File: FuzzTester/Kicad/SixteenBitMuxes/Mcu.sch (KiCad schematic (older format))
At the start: 20 parts, among them J10 Key Pad JST XH, J11 LCD JST XH, J12 Bypass Switch JST XH, J7 Boot Reset PinHeader, J8 SPI Test PinHeader, J9 SWD_PinHeader, U3 STM32F103C8Tx, Y1 8MHz

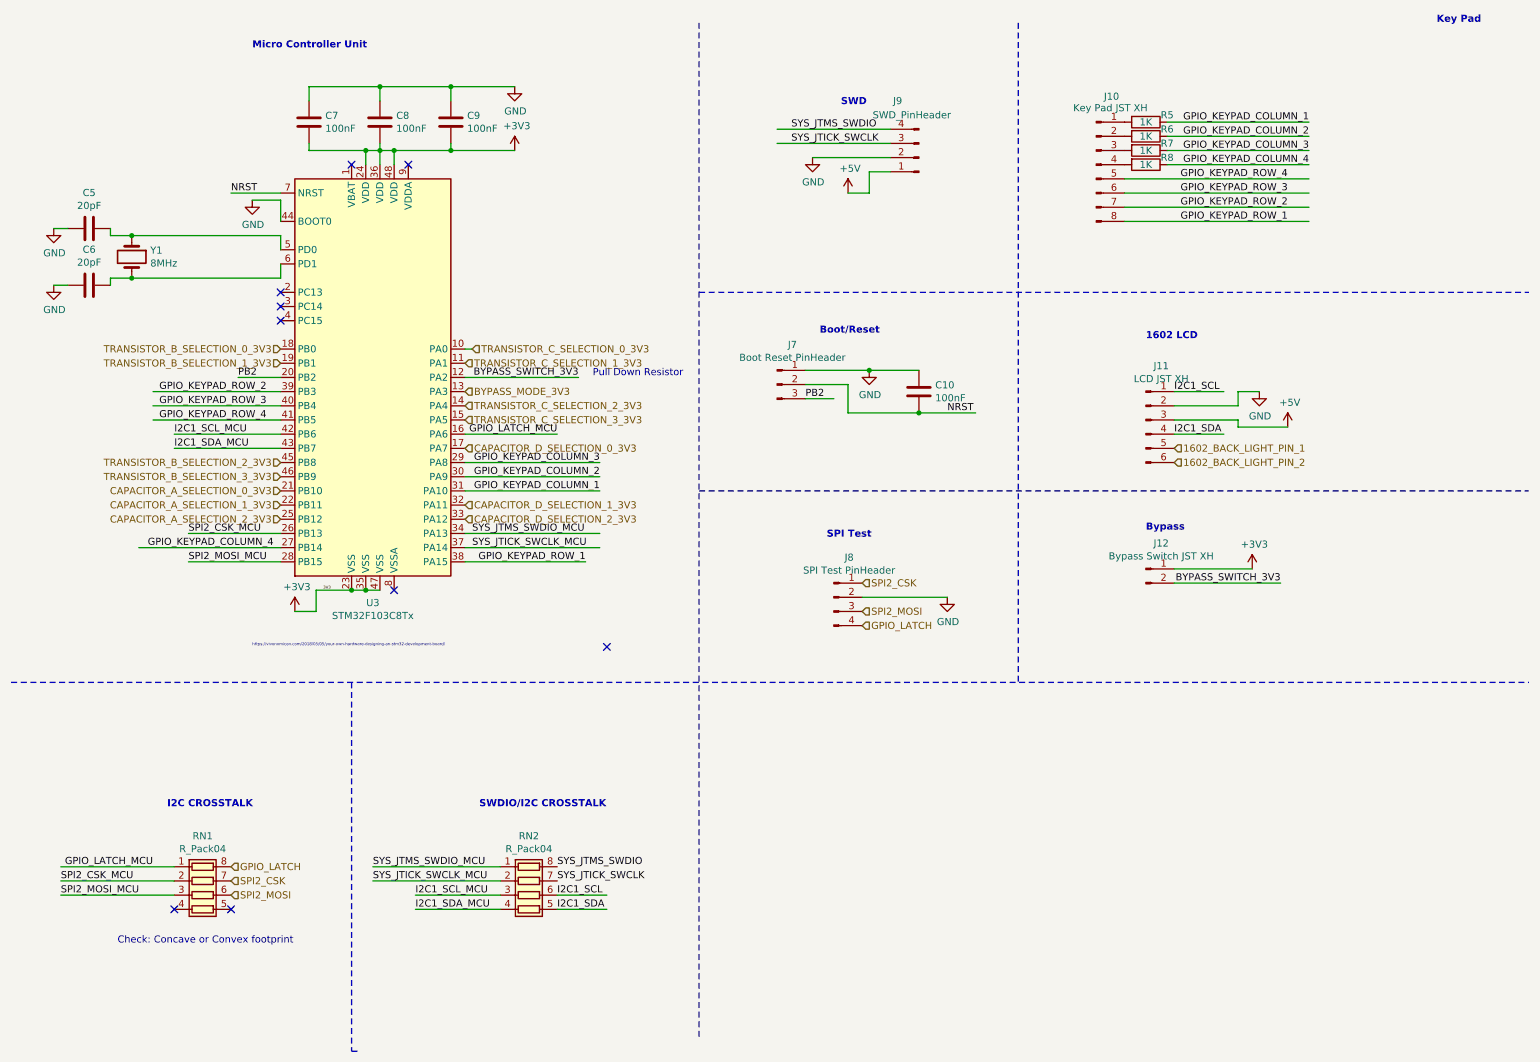
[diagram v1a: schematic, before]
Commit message: Finished (but not beautiful) PCB without SPI and most 8 channel multiplexers.
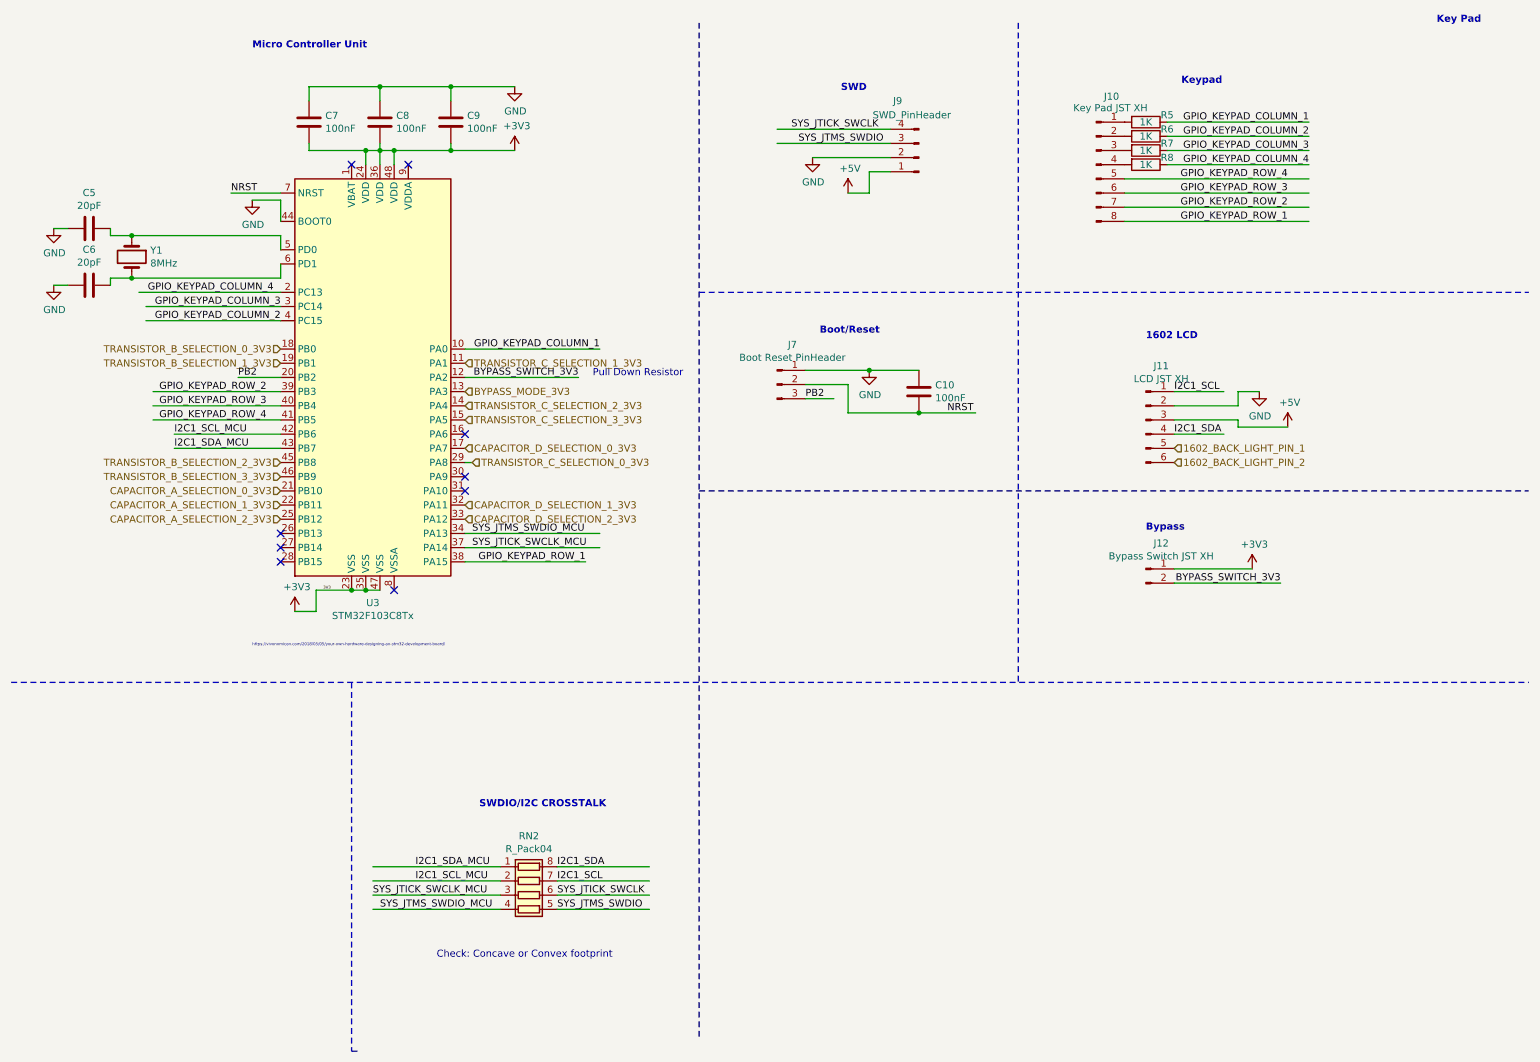
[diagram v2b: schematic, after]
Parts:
- removed J8: SPI Test PinHeader, Connector_PinHeader_2.54mm:PinHeader_1x04_P2.54mm_Vertical, symbol Connector:Conn_01x04_Male
- removed RN1: R_Pack04, Resistor_SMD:R_Array_Convex_4x0603, symbol Device:R_Pack04
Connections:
- net labels removed: GPIO_LATCH, GPIO_LATCH_MCU, SPI2_CSK, SPI2_CSK_MCU, SPI2_MOSI, SPI2_MOSI_MCU
- wire segments 94 -> 89
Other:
- note added: "Keypad\n\n\n"
- note removed: "I2C CROSSTALK\n\n\n"
- note removed: "SPI Test\n\n\n"
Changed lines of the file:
@@
 $Descr A4 11693 8268
 encoding utf-8
-Sheet 6 9
+Sheet 9 9
 Title "Guitar Pedal Effect Fuzz Digitally Controlled"
 Date "2020-04-07"
@@
 	-1   0    0    1
 $EndComp
+Text Label 6050 1400 0    50   ~ 0
+SYS_JTMS_SWDIO
 Text Label 6000 1300 0    50   ~ 0
-SYS_JTMS_SWDIO
-Text Label 6000 1400 0    50   ~ 0
 SYS_JTICK_SWCLK
 $Comp
@@
 Text Notes 6200 2750 0    50   ~ 10
 Boot/Reset\n
-$Comp
-L Connector:Conn_01x04_Male J?
-U 1 1 5EBB7B0E
-P 6300 4600
-AR Path="/5EBB7B0E" Ref="J?"  Part="1"
-AR Path="/5E8F7778/5EBB7B0E" Ref="J?"  Part="1"
-AR Path="/5E8BDF21/5EBB7B0E" Ref="J8"  Part="1"
-F 0 "J8" H 6408 4881 50  0000 C CNN
-F 1 "SPI Test PinHeader" H 6408 4790 50  0000 C CNN
-F 2 "Connector_PinHeader_2.54mm:PinHeader_1x04_P2.54mm_Vertical" H 6300 4600 50  0001 C CNN
-F 3 "~" H 6300 4600 50  0001 C CNN
-	1    6300 4600
-	1    0    0    -1
-$EndComp
-$Comp
-L power:GND #PWR?
-U 1 1 5EBB7B14
-P 7100 4600
-AR Path="/5EBB7B14" Ref="#PWR?"  Part="1"
-AR Path="/5E8F7778/5EBB7B14" Ref="#PWR?"  Part="1"
-AR Path="/5E8BDF21/5EBB7B14" Ref="#PWR023"  Part="1"
-F 0 "#PWR023" H 7100 4350 50  0001 C CNN
-F 1 "GND" H 7105 4427 50  0000 C CNN
-F 2 "" H 7100 4600 50  0001 C CNN
-F 3 "" H 7100 4600 50  0001 C CNN
-	1    7100 4600
-	1    0    0    -1
-$EndComp
-Text Notes 6250 4350 0    50   ~ 10
-SPI Test\n\n\n
-Text HLabel 6500 4500 2    50   Input ~ 0
-SPI2_CSK
-Text HLabel 6500 4700 2    50   Input ~ 0
-SPI2_MOSI
-Text HLabel 6500 4800 2    50   Input ~ 0
-GPIO_LATCH
-Text Notes 6350 1300 0    50   ~ 10
+Text Notes 6350 1200 0    50   ~ 10
 SWD\n\n\n
 NoConn ~ 2900 1550
@@
 	8700 3350 9150 3350
 Wire Wire Line
-	2400 4250 1400 4250
-Wire Wire Line
-	3700 3850 4650 3850
-Wire Wire Line
-	4650 3750 3700 3750
-Wire Wire Line
-	3700 3650 4650 3650
+	2400 2450 1400 2450
+Wire Wire Line
+	3700 2850 4650 2850
+Wire Wire Line
+	2400 2650 1450 2650
+Wire Wire Line
+	1450 2550 2400 2550
 Text Label 9500 1850 2    50   ~ 0
 GPIO_KEYPAD_ROW_2
@@
 $EndComp
 Wire Wire Line
-	7100 4600 6500 4600
-Wire Wire Line
 	9150 3400 9150 3350
 Wire Wire Line
@@
 Text Label 2300 3350 2    50   ~ 0
 GPIO_KEYPAD_ROW_4
-Text Label 4650 3850 2    50   ~ 0
+Text Label 4650 2850 2    50   ~ 0
 GPIO_KEYPAD_COLUMN_1
 Text Label 2300 3250 2    50   ~ 0
 GPIO_KEYPAD_ROW_3
-Text Label 4650 3750 2    50   ~ 0
+Text Label 2400 2650 2    50   ~ 0
 GPIO_KEYPAD_COLUMN_2
-Text Label 4650 3650 2    50   ~ 0
+Text Label 2400 2550 2    50   ~ 0
 GPIO_KEYPAD_COLUMN_3
 Text Label 2300 3150 2    50   ~ 0
@@
 Text Label 4550 4350 2    50   ~ 0
 GPIO_KEYPAD_ROW_1
-Text Label 2350 4250 2    50   ~ 0
+Text Label 2350 2450 2    50   ~ 0
 GPIO_KEYPAD_COLUMN_4
 Text Label 9500 1650 2    50   ~ 0
@@
 	0    1    1    0
 $EndComp
-Text Label 3050 6500 0    50   ~ 0
-SYS_JTMS_SWDIO_MCU
-Text Label 3050 6600 0    50   ~ 0
+Text Label 3050 6700 0    50   ~ 0
 SYS_JTICK_SWCLK_MCU
+Text Label 4350 6800 0    50   ~ 0
+SYS_JTMS_SWDIO
+Text Label 4350 6700 0    50   ~ 0
+SYS_JTICK_SWCLK
+Wire Wire Line
+	3700 4150 4650 4150
+Wire Wire Line
+	3700 4250 4650 4250
+Wire Wire Line
+	3950 6600 3050 6600
+Wire Wire Line
+	3050 6500 3950 6500
+Text Label 4350 6600 0    50   ~ 0
+I2C1_SCL
 Text Label 4350 6500 0    50   ~ 0
-SYS_JTMS_SWDIO
-Text Label 4350 6600 0    50   ~ 0
-SYS_JTICK_SWCLK
-Text Label 850  6700 0    50   ~ 0
-SPI2_MOSI_MCU
-Text Label 1750 4350 0    50   ~ 0
-SPI2_MOSI_MCU
-Text Label 1750 4150 0    50   ~ 0
-SPI2_CSK_MCU
-Wire Wire Line
-	1750 4150 2400 4150
-Text Label 850  6600 0    50   ~ 0
-SPI2_CSK_MCU
-Wire Wire Line
-	1750 4350 2400 4350
-Wire Wire Line
-	3700 4150 4650 4150
-Wire Wire Line
-	3700 4250 4650 4250
-Text Label 4350 3450 2    50   ~ 0
-GPIO_LATCH_MCU
-Wire Wire Line
-	3700 3450 4350 3450
-Wire Wire Line
-	3950 6800 3350 6800
-Text Label 3350 6700 0    50   ~ 0
-I2C1_SCL_MCU
-Text Label 3350 6800 0    50   ~ 0
-I2C1_SDA_MCU
-Wire Wire Line
-	3350 6700 3950 6700
-Wire Wire Line
-	3950 6600 3050 6600
-Wire Wire Line
-	3050 6500 3950 6500
-Wire Wire Line
-	4700 6800 4350 6800
-Text Label 4350 6700 0    50   ~ 0
-I2C1_SCL
-Text Label 4350 6800 0    50   ~ 0
 I2C1_SDA
-Wire Wire Line
-	4350 6700 4700 6700
 Text Notes 3800 6250 0    50   ~ 10
 SWDIO/I2C CROSSTALK\n\n\n
@@
 Wire Wire Line
 	1350 2350 2400 2350
-Text Notes 1250 7050 0    50   ~ 0
-Check: Concave or Convex footprint
-Text Notes 1600 6250 0    50   ~ 10
-I2C CROSSTALK\n\n\n
-NoConn ~ 2050 6800
-NoConn ~ 1650 6800
-Wire Wire Line
-	1650 6700 850  6700
-Wire Wire Line
-	850  6600 1650 6600
-Wire Wire Line
-	1650 6500 850  6500
-Text HLabel 2050 6500 2    50   Input ~ 0
-GPIO_LATCH
-Text Label 1500 6500 2    50   ~ 0
-GPIO_LATCH_MCU
-Text HLabel 2050 6600 2    50   Input ~ 0
-SPI2_CSK
-Text HLabel 2050 6700 2    50   Input ~ 0
-SPI2_MOSI
-$Comp
-L Device:R_Pack04 RN1
-U 1 1 5EA7B481
-P 1850 6700
-F 0 "RN1" V 1433 6700 50  0000 C CNN
-F 1 "R_Pack04" V 1524 6700 50  0000 C CNN
-F 2 "Resistor_SMD:R_Array_Convex_4x0603" V 2125 6700 50  0001 C CNN
-F 3 "~" H 1850 6700 50  0001 C CNN
-	1    1850 6700
-	0    1    1    0
-$EndComp
 Wire Wire Line
 	3000 4550 3100 4550
@@
 	1    0    0    -1
 $EndComp
-NoConn ~ 2400 2450
-NoConn ~ 2400 2550
-NoConn ~ 2400 2650
-NoConn ~ 4700 4950
+NoConn ~ 2400 4150
 Text HLabel 2400 2850 0    50   Input ~ 0
 TRANSISTOR_B_SELECTION_0_3V3
@@
 Text HLabel 2400 4050 0    50   Input ~ 0
 CAPACITOR_A_SELECTION_2_3V3
-Text HLabel 3750 2850 2    50   Input ~ 0
+Text HLabel 3750 3650 2    50   Input ~ 0
 TRANSISTOR_C_SELECTION_0_3V3
 Text HLabel 3700 2950 2    50   Input ~ 0
@@
 CAPACITOR_D_SELECTION_2_3V3
 Wire Wire Line
-	3700 2850 3750 2850
+	3700 3650 3750 3650
+Text Notes 8750 1150 0    50   ~ 10
+Keypad\n\n\n
+Text Label 3350 6600 0    50   ~ 0
+I2C1_SCL_MCU
+Text Label 3350 6500 0    50   ~ 0
+I2C1_SDA_MCU
+Text Label 3100 6800 0    50   ~ 0
+SYS_JTMS_SWDIO_MCU
+Wire Wire Line
+	4350 6600 5000 6600
+Wire Wire Line
+	4350 6500 5000 6500
+Wire Wire Line
+	4350 6700 5000 6700
+Wire Wire Line
+	4350 6800 5000 6800
+Wire Wire Line
+	3050 6800 3950 6800
+Wire Wire Line
+	3050 6700 3950 6700
+NoConn ~ 3700 3450
+NoConn ~ 3700 3750
+NoConn ~ 3700 3850
+NoConn ~ 2400 4250
+Text Notes 3500 7150 0    50   ~ 0
+Check: Concave or Convex footprint
+NoConn ~ 2400 4350
 $EndSCHEMATC
